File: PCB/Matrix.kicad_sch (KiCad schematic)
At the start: 139 parts, among them SW1 CPG151101S11, SW10 CPG151101S11, SW11 CPG151101S11, SW12 CPG151101S11, SW13 CPG151101S11, SW14 CPG151101S11, SW15 CPG151101S11, SW16 CPG151101S11, SW17 CPG151101S11, SW18 CPG151101S11, SW19 CPG151101S11, SW2 CPG151101S11, SW20 CPG151101S11, SW21 CPG151101S11, SW22 CPG151101S11, SW23 CPG151101S11, SW24 CPG151101S11, SW25 CPG151101S11, SW26 CPG151101S11, SW27 CPG151101S11, SW28 CPG151101S11, SW29 CPG151101S11, SW3 CPG151101S11, SW30 CPG151101S11, SW31 CPG151101S11, SW32 CPG151101S11, SW33 CPG151101S11, SW34 CPG151101S11, SW35 CPG151101S11, SW36 CPG151101S11, SW37 CPG151101S11, SW38 CPG151101S11, SW39 CPG151101S11, SW4 CPG151101S11, SW40 CPG151101S11, SW41 CPG151101S11, SW42 CPG151101S11, SW43 CPG151101S11, SW44 CPG151101S11, SW45 CPG151101S11, SW46 CPG151101S11, SW47 CPG151101S11, SW48 CPG151101S11, SW49 CPG151101S11, SW5 CPG151101S11, SW50 CPG151101S11, SW51 CPG151101S11, SW52 CPG151101S11, SW53 CPG151101S11, SW54 CPG151101S11, SW55 CPG151101S11, SW56 CPG151101S11, SW57 CPG151101S11, SW58 CPG151101S11, SW59 CPG151101S11, SW6 CPG151101S11, SW60 CPG151101S11, SW61 CPG151101S11, SW62 CPG151101S11, SW63 CPG151101S11, SW64 CPG151101S11, SW67 PER56, SW7 CPG151101S11, SW8 CPG151101S11, SW9 CPG151101S11, U10 74HC595, U11 74HC595

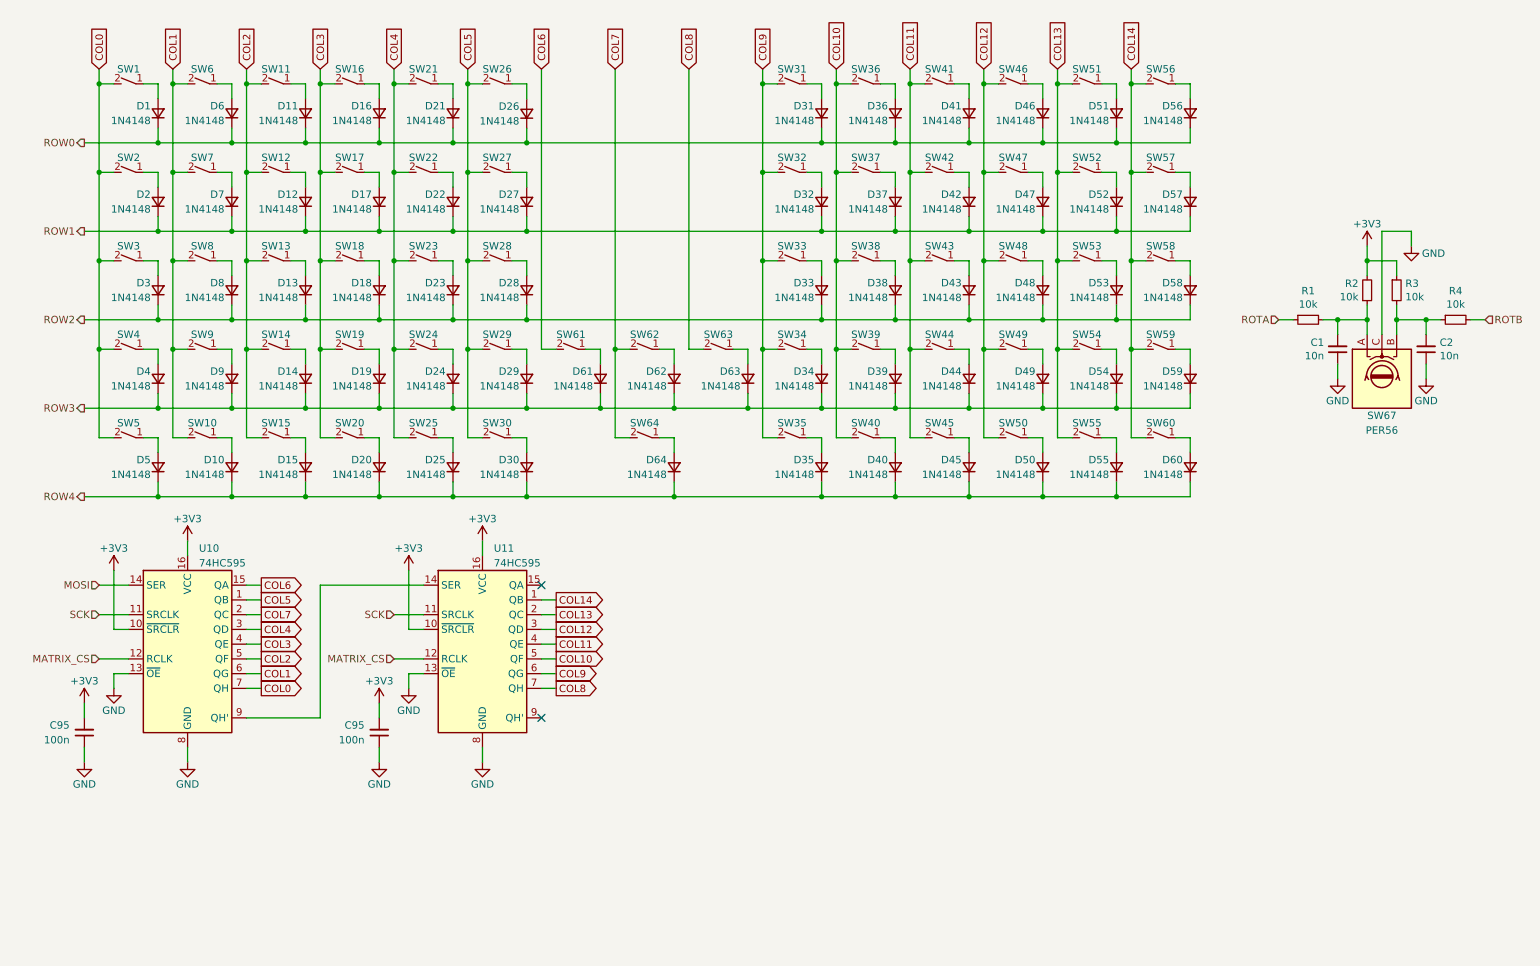
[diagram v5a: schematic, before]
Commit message: Added thumb wheel encoder in 2u slot.
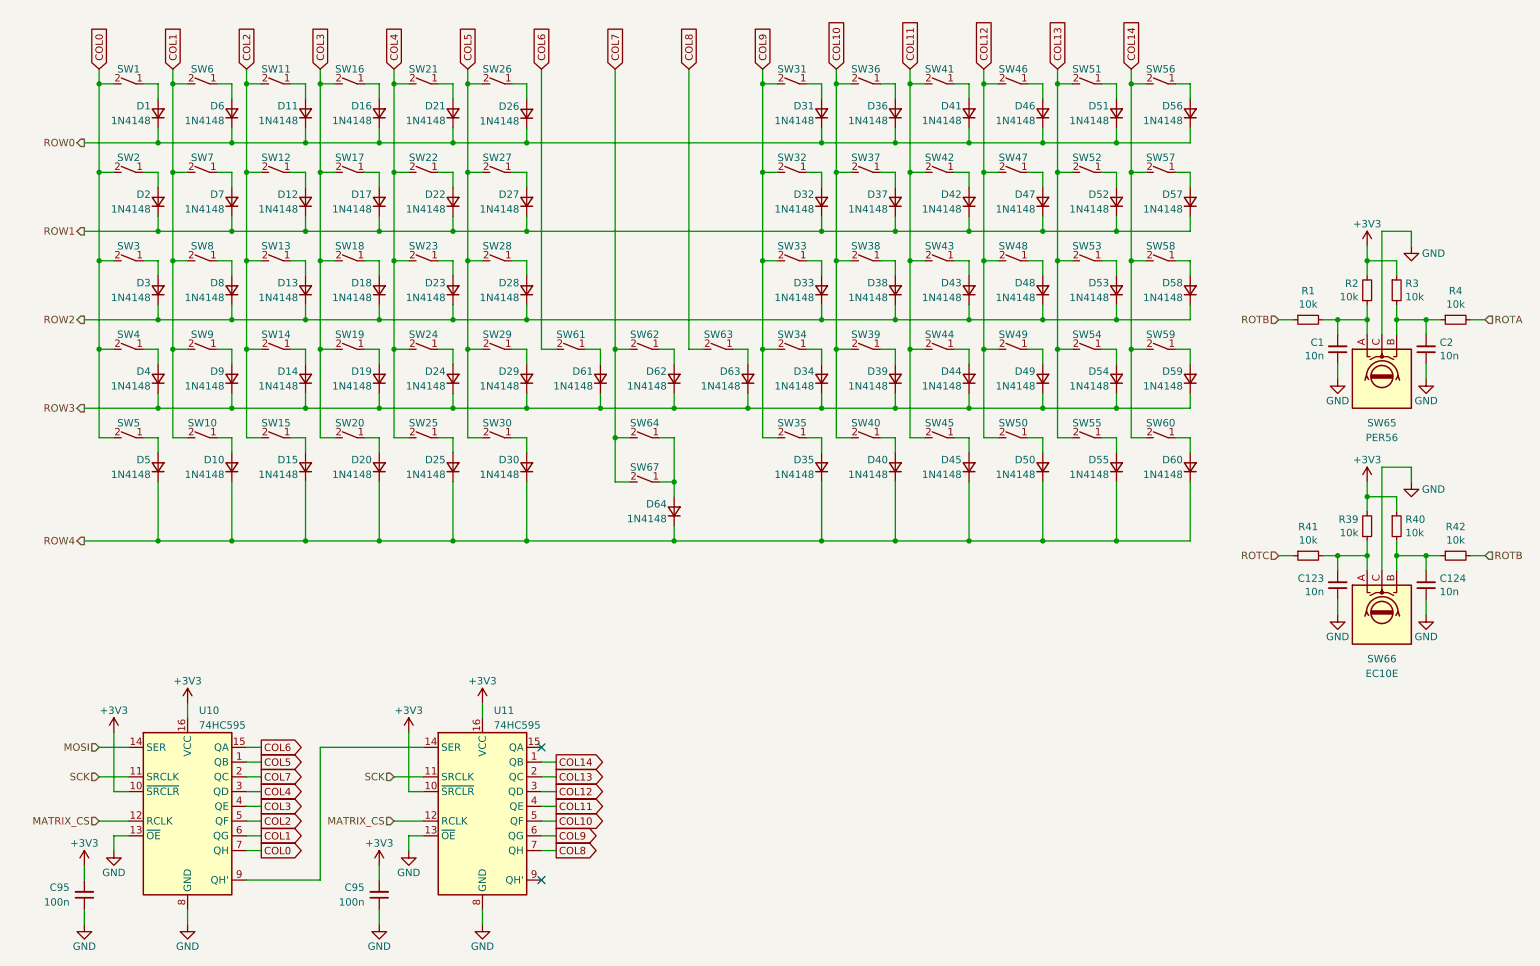
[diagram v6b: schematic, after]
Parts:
- added C123, C124: 10n, Capacitor_SMD:C_0402_1005Metric, symbol Device:C_Small
- added R39, R40, R41, R42: 10k, Resistor_SMD:R_0402_1005Metric, symbol Device:R_Small
- added SW66: EC10E, Honeydew:EC10E, symbol Device:RotaryEncoder
- added SW67: (no value), Honeydew:D2F-01F, symbol Cantaloupe:SW_SPST_Small
- renumbered SW67 to SW65
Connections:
- net +3V3: now also R39.2, R40.1
- net COL7: now also SW67.2 (B)
- net GND: now also C123.1, C124.1, SW66.C
- net ROTA: now also R4.2; no longer R1.1
- net ROTB: now also R1.1, R42.2; no longer R4.2
- net at D64.2 (A), SW64.1 (A): now also SW67.1 (A)
- new net: C124.2, R40.2, R42.1, SW66.B
- new net: C123.2, R39.1, R41.2, SW66.A
- new net ROTC: R41.1
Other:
- moved on the sheet: C95, D64, U10, U11

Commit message: Updated BOM. Added new tentative plate file.
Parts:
- SW67: value (none) -> ~
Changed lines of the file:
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@@
       (effects (font (size 1.27 1.27)))
     )
-    (property "Value" "" (at 121.92 101.6 0)
+    (property "Value" "~" (at 121.92 101.6 0)
       (effects (font (size 1.524 1.524)) hide)
     )
